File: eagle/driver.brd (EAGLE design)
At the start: 101.6 x 76.2 mm, 39 parts, among them IC1 XMEGA128A1, IC10 ST95P08M, IC11 ST95P08M, IC12 ST95P08M, IC13 ST95P08M, IC14 ST95P08M, IC15 ST95P08M, IC16 74AHC1G32DBV, IC17 74AHC1G32DBV, IC18 74AHC1G08DBV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

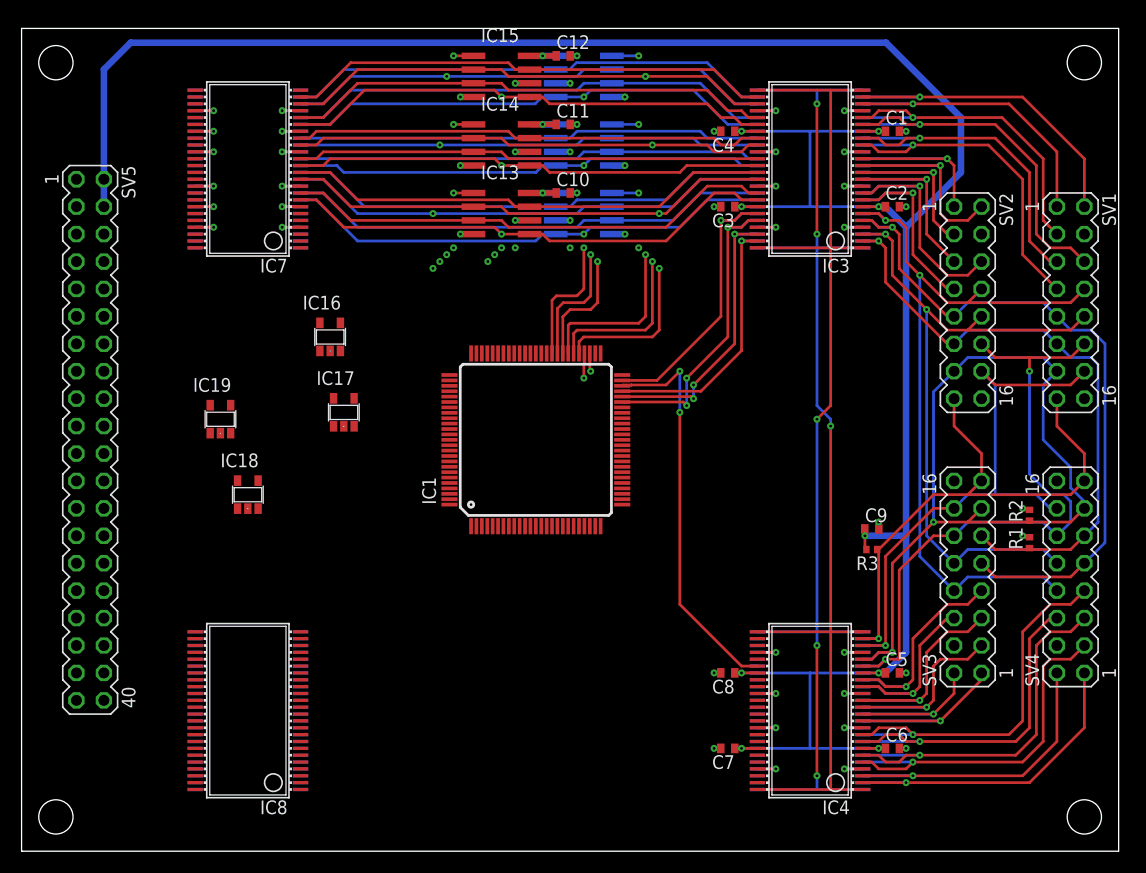
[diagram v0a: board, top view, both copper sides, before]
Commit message: driver board layout progress
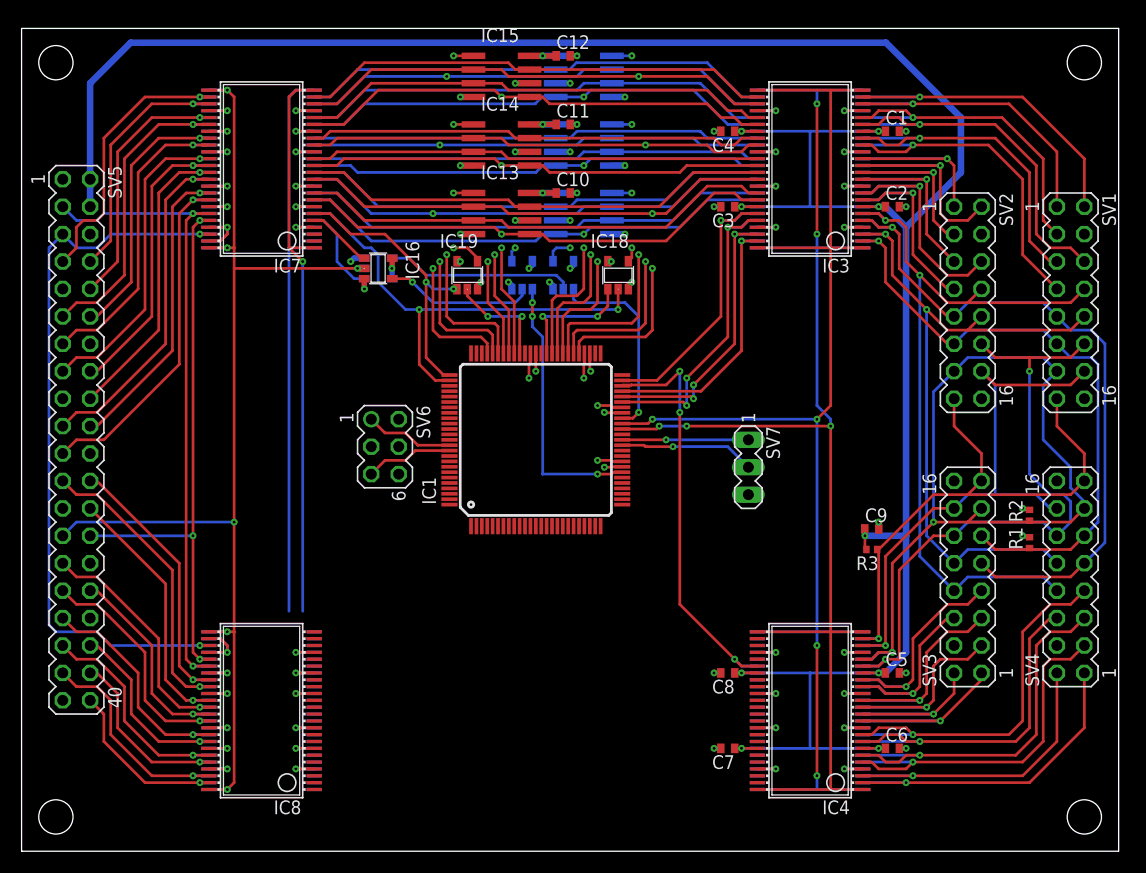
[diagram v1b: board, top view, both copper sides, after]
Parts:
- added IC20, IC21: 74AHC1G02DBV, 74xx-little-us:SOT23-5
- added SV6: (no value), con-lstb:MA03-2
- added SV7: (no value), con-lstb:MA03-1
- moved IC18 39.9 mm to (55.2, 53.3)
- moved IC19 26.5 mm to (41.3, 53.3)
- moved IC17 13.7 mm to (33.0, 54.0), flipped to the bottom, turned to 90 degrees
- moved IC16 7.75 mm to (33.0, 54.0), turned to 270 degrees
- moved IC6 1.27 mm to (22.2, 63.5)
- moved IC7 1.27 mm to (22.2, 62.9)
- moved IC8 1.27 mm to (22.2, 12.7)
- moved IC9 1.27 mm to (22.2, 13.3)
- moved SV5 1.27 mm to (5.08, 38.1)
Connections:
- net N$103 renamed OE
- net N$104 renamed LAT
- removed net N$105: IC4.29, IC5.44
- new net CLK: IC4.29
- new net CLKA: IC1.32, IC21.1
- new net CLKB: IC1.42, IC20.1
- new net CS0: IC10.1, IC11.1, IC12.1, IC18.4
- new net CS1: IC13.1, IC14.1, IC15.1, IC19.4
- new net N$103: IC5.44
- new net N$106: IC8.40, IC9.33, SV5.33
- new net N$108: IC8.43, IC9.30, SV5.35
- new net N$110: IC17.1, IC6.20
- new net N$111: IC8.46, IC9.27, SV5.37
- new net N$113: IC16.1, IC7.5
- new net N$118: IC8.41, IC9.32, SV5.36
- new net N$34: IC6.33, IC7.40, SV5.20
- new net N$46: IC16.4, IC21.2
- new net N$52: IC6.38, IC7.35, SV5.15
- new net SCLK0: IC10.6, IC11.6, IC12.6, IC20.4
- new net SCLK1: IC13.6, IC14.6, IC15.6, IC21.4
- new net VSYNC0: IC1.77, IC18.2, IC6.19
- new net VSYNC1: IC1.76, IC19.1, IC7.6
- net GND: now also IC20.3, IC21.3, IC6.26, IC7.47, IC8.26, IC9.47, SV6.6, SV7.3
- net N$102: now also IC8.38, IC9.35, SV5.31; no longer IC10.6, IC11.6, IC12.6
- net N$109: now also IC8.44, IC9.29, SV5.38; no longer IC13.1, IC14.1, IC15.1
- net N$112: now also IC8.47, IC9.26, SV5.40; no longer IC13.6, IC14.6, IC15.6
- net N$16: now also IC1.40
- net N$19: now also IC1.41
- net N$30: now also IC6.32, IC7.41, SV5.21; no longer IC10.2, IC2.46, IC6.3
- net N$40: now also IC6.35, IC7.38, SV5.19; no longer IC11.2, IC2.40, IC6.9
- net N$42: now also IC17.4, IC20.2; no longer IC10.1, IC11.1, IC12.1
- net N$44: now also IC6.36, IC7.37, SV5.18; no longer IC12.2, IC2.35, IC6.14
- net N$50: now also IC6.37, IC7.36, SV5.16; no longer IC15.5, IC3.30, IC7.19
- net N$54: now also IC6.40, IC7.33, SV5.13; no longer IC14.5, IC3.36, IC7.13
- net N$58: now also IC6.41, IC7.32, SV5.12; no longer IC13.5, IC3.41, IC7.8
- net N$59: now also IC6.43, IC7.30, SV5.11; no longer IC6.23, IC7.2
- net N$60: now also IC6.44, IC7.29, SV5.10; no longer IC6.22, IC7.3
- net N$61: now also IC6.46, IC7.27, SV5.8; no longer IC6.20, IC7.5
- net N$62: now also IC6.47, IC7.26, SV5.7; no longer IC6.19, IC7.6
- net N$87: now also IC1.89, SV6.1; no longer IC8.23, IC9.2
- net N$88: now also IC1.90, SV6.5; no longer IC8.22, IC9.3
- net N$89: now also IC1.38, SV7.1; no longer IC8.20, IC9.5
- net N$90: now also IC1.37, SV7.2; no longer IC8.19, IC9.6
- net N$91: now also IC8.32, IC9.41, SV5.24; no longer IC6.26, IC7.47
- net N$92: now also IC8.27, IC9.46, SV5.5
- net N$93: now also IC8.29, IC9.44, SV5.28
- net N$94: now also IC8.30, IC9.43, SV5.3
- net N$95: now also IC8.33, IC9.40, SV5.23; no longer IC8.26, IC9.47
- net N$96: now also IC8.35, IC9.38, SV5.26; no longer IC8.27, IC9.46
- net N$97: now also IC8.36, IC9.37, SV5.29; no longer IC8.29, IC9.44
- net N$98: now also IC8.37, IC9.36, SV5.32; no longer IC8.30, IC9.43
- net N$99: now also IC16.2, IC17.2, SV5.27
- net PH6: now also IC18.1
- net PJ1: now also IC19.2
- net PJ2: now also IC13.5, IC3.41, IC7.8
- net PJ3: now also IC14.5, IC3.36, IC7.13
- net PJ4: now also IC15.5, IC3.30, IC7.19
- net PJ5: now also IC10.2, IC2.46, IC6.3
- net PJ6: now also IC11.2, IC2.40, IC6.9
- net PJ7: now also IC12.2, IC2.35, IC6.14
- net VCC: now also IC20.5, IC21.5, SV6.2
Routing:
- net N$99: track 0.00 -> 109.2 mm, vias 0 -> 6
- net PJ5: track 0.00 -> 73.5 mm, vias 0 -> 2
- net N$92: track 0.00 -> 68.6 mm, vias 0 -> 2
- net PJ4: track 0.00 -> 68.6 mm, vias 0 -> 2
- net PJ6: track 0.00 -> 65.1 mm, vias 0 -> 2
- net N$94: track 0.00 -> 61.2 mm, vias 0 -> 2
- net PJ7: track 0.00 -> 60.9 mm, vias 0 -> 2
- net PJ3: track 0.00 -> 60.3 mm, vias 0 -> 2
- net PJ2: track 0.00 -> 56.3 mm, vias 0 -> 2
- net N$93: track 0.00 -> 54.0 mm, vias 0 -> 3
- net N$100: track 0.00 -> 53.1 mm, vias 0 -> 1
- net N$101: track 0.00 -> 52.6 mm
- net GND: track 99.5 -> 147.6 mm, vias 45 -> 62
- net VSYNC0: track 0.00 -> 43.7 mm, vias 0 -> 2
- net N$50: track 60.7 -> 27.4 mm, vias 2 -> 1
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
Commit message: board layout progress
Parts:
- removed IC18, IC19: 74AHC1G08DBV, 74xx-little-us:SOT23-5
- moved IC20 0.64 mm to (50.2, 52.7)
- moved IC21 0.64 mm to (46.4, 52.7)
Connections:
- removed net CLK: IC4.29
- removed net CS0: IC10.1, IC11.1, IC12.1, IC18.4
- removed net CS1: IC13.1, IC14.1, IC15.1, IC19.4
- removed net N$103: IC5.44
- net CLKA: now also IC4.29
- net CLKB: now also IC5.44
- net GND: no longer IC18.3, IC19.3
- net LAT: now also IC1.35
- net N$100: now also IC1.78
- net N$101: now also IC1.79
- net N$99: now also IC1.92
- net OE: now also IC1.36
- net PH6: no longer IC18.1
- net PJ1: no longer IC19.2
- net VCC: no longer IC18.5, IC19.5
- net VSYNC0: now also IC10.1, IC11.1, IC12.1; no longer IC18.2
- net VSYNC1: now also IC13.1, IC14.1, IC15.1; no longer IC19.1
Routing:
- net LAT: track 0.00 -> 29.3 mm, vias 0 -> 3
- net OE: track 0.00 -> 28.6 mm, vias 0 -> 3
- net CS1: track 26.2 -> 0.00 mm, vias 4 -> 0
- net VSYNC0: track 43.7 -> 68.8 mm, vias 2 -> 5
- net CS0: track 24.7 -> 0.00 mm, vias 4 -> 0
- net VSYNC1: track 26.3 -> 51.0 mm, vias 2 -> 4
- net N$99: track 109.2 -> 130.2 mm
- net N$101: track 52.6 -> 67.4 mm, vias 0 -> 1
- net N$100: track 53.1 -> 66.7 mm, vias 1 -> 2
- net VCC: track 51.8 -> 65.2 mm, vias 20 -> 24
- net PH6: track 11.6 -> 0.00 mm, vias 2 -> 0
- net PJ1: track 10.0 -> 0.00 mm, vias 2 -> 0
- net GND: track 147.6 -> 156.5 mm, vias 62 -> 66
- net CLKB: track 18.3 -> 26.5 mm
- net PH5: track 57.6 -> 56.5 mm
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
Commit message: board layout progress
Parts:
- added IC18, IC19: 74AHC1G125DBV, 74xx-little-us:SOT23-5
- added IC22, IC23, IC24, IC25: ST95P08M, st-microelectronics:SO08
- added R4, R5: 33k, rcl:R0402
- IC16, IC17: value 74AHC1G32DBV -> 74AHC1G02DBV
- IC20, IC21: value 74AHC1G02DBV -> ST95P08M; device 74xx-little-us:SOT23-5 -> st-microelectronics:SO08
- moved IC21 42.0 mm to (44.5, 10.8), flipped to the top, turned to 270 degrees
- moved IC20 36.0 mm to (44.5, 17.1), flipped to the top, turned to 270 degrees
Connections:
- removed net CLKA: IC1.32, IC21.1, IC4.29
- removed net CLKB: IC1.42, IC20.1, IC5.44
- removed net N$100: IC1.78, IC7.1, IC7.24, IC9.1, IC9.24
- removed net N$101: IC1.79, IC6.1, IC6.24, IC8.1, IC8.24
- removed net N$75: IC5.26, IC9.23
- removed net N$77: IC5.29, IC9.20
- removed net N$79: IC5.32, IC9.17
- removed net N$81: IC5.35, IC9.14
- removed net N$83: IC5.37, IC9.12
- removed net N$85: IC5.40, IC9.9
- new net CLK_EN0: IC1.80, IC19.1
- new net CLK_EN1: IC1.81, IC18.1
- new net N$48: IC1.78, IC6.1, IC6.24, IC9.1, IC9.24
- new net N$56: IC1.79, IC7.1, IC7.24, IC8.1, IC8.24
- new net PB0: IC1.5, IC25.5, IC5.37, IC9.12
- new net PB1: IC1.6, IC24.5, IC5.32, IC9.17
- new net PB2: IC1.7, IC23.5, IC5.26, IC9.23
- new net PB3: IC1.8, IC25.2, IC5.40, IC9.9
- new net PB4: IC1.9, IC24.2, IC5.35, IC9.14
- new net PB5: IC1.10, IC23.2, IC5.29, IC9.20
- new net PB6: IC1.11
- new net PB7: IC1.12
- new net VSYNC2: IC1.1, IC20.1, IC21.1, IC22.1, IC8.19
- new net VSYNC3: IC1.2, IC23.1, IC24.1, IC25.1, IC9.6
- net GND: now also IC18.3, IC19.3, IC20.4, IC21.4, IC22.4, IC23.4, IC24.4, IC25.4; no longer IC20.3, IC21.3
- net N$110: now also R4.1
- net N$113: now also R5.1
- net N$16: now also IC3.1, IC3.24, IC3.25, IC3.48; no longer IC2.1, IC2.24, IC2.25, IC2.48
- net N$19: now also IC2.1, IC2.24, IC2.25, IC2.48; no longer IC3.1, IC3.24, IC3.25, IC3.48
- net N$42: now also IC16.4, IC18.2; no longer IC17.4, IC20.2
- net N$46: now also IC17.4, IC19.2; no longer IC16.4, IC21.2
- net N$63: now also IC22.5
- net N$64: now also IC22.3
- net N$65: now also IC22.7
- net N$66: now also IC22.2
- net N$67: now also IC21.5
- net N$68: now also IC21.3
- net N$69: now also IC21.2
- net N$70: now also IC21.7
- net N$71: now also IC20.5
- net N$72: now also IC20.3
- net N$73: now also IC20.2
- net N$74: now also IC20.7
- net N$76: now also IC23.3
- net N$78: now also IC23.7
- net N$80: now also IC24.3
- net N$82: now also IC24.7
- net N$84: now also IC25.3
- net N$86: now also IC25.7
- net SCLK0: now also IC1.32, IC19.4, IC23.6, IC24.6, IC25.6, IC5.44; no longer IC20.4
- net SCLK1: now also IC1.42, IC18.4, IC20.6, IC21.6, IC22.6, IC4.29; no longer IC21.4
- net VCC: now also IC18.5, IC19.5, IC20.8, IC21.8, IC22.8, IC23.8, IC24.8, IC25.8, R4.2, R5.2; no longer IC20.5, IC21.5
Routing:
- net SCLK1: track 21.2 -> 127.9 mm, vias 4 -> 14
- net SCLK0: track 22.5 -> 116.8 mm, vias 4 -> 9
- net N$56: track 0.00 -> 88.3 mm, vias 0 -> 3
- net N$48: track 0.00 -> 88.2 mm, vias 0 -> 1
- net PB2: track 0.00 -> 75.1 mm, vias 0 -> 2
- net PB5: track 0.00 -> 70.8 mm, vias 0 -> 2
- net N$101: track 67.4 -> 0.00 mm, vias 1 -> 0
- net N$100: track 66.7 -> 0.00 mm, vias 2 -> 0
- net PB1: track 0.00 -> 66.7 mm, vias 0 -> 2
- net PB4: track 0.00 -> 62.2 mm, vias 0 -> 2
- net VSYNC3: track 0.00 -> 61.3 mm, vias 0 -> 4
- net PB0: track 0.00 -> 60.9 mm, vias 0 -> 2
- net PB3: track 0.00 -> 56.6 mm, vias 0 -> 2
- net VSYNC2: track 0.00 -> 45.0 mm, vias 0 -> 3
- net N$63: track 0.00 -> 44.7 mm
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
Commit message: board layout progress
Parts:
- moved R5 0.90 mm to (29.2, 56.5)
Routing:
- net PH0: track 62.8 -> 59.4 mm
- net PH1: track 67.3 -> 64.2 mm
- net PH2: track 75.0 -> 72.0 mm
- net PJ7: track 60.9 -> 58.7 mm
- net PJ6: track 64.9 -> 62.9 mm
- net PJ5: track 73.2 -> 71.3 mm
- net VCC/2: track 241.5 -> 242.1 mm

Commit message: board layout progress
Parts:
- added C13, C14, C15: 100n, rcl:C0402
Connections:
- removed net N$63: IC22.5, IC4.47, IC8.2
- removed net N$66: IC22.2, IC4.44, IC8.5
- removed net N$67: IC21.5, IC4.41, IC8.8
- removed net N$69: IC21.2, IC4.38, IC8.11
- removed net N$71: IC20.5, IC4.36, IC8.13
- removed net N$73: IC20.2, IC4.33, IC8.16
- new net PC0: IC1.15, IC22.2, IC4.44, IC8.5
- new net PC1: IC1.16, IC21.2, IC4.38, IC8.11
- new net PC2: IC1.17, IC20.2, IC4.33, IC8.16
- new net PC3: IC1.18, IC22.5, IC4.47, IC8.2
- new net PC4: IC1.19, IC21.5, IC4.41, IC8.8
- new net PC5: IC1.20, IC20.5, IC4.36, IC8.13
- new net PC6: IC1.21
- new net PC7: IC1.22
- net GND: now also C13.2, C14.2, C15.2
- net VCC: now also C13.1, C14.1, C15.1
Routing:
- net PC3: track 0.00 -> 76.2 mm, vias 0 -> 2
- net PC0: track 0.00 -> 71.5 mm, vias 0 -> 2
- net PC4: track 0.00 -> 68.3 mm, vias 0 -> 2
- net PC1: track 0.00 -> 62.9 mm, vias 0 -> 2
- net PC5: track 0.00 -> 62.0 mm, vias 0 -> 2
- net PC2: track 0.00 -> 57.9 mm, vias 0 -> 2
- net N$63: track 44.7 -> 0.00 mm
- net N$66: track 44.2 -> 0.00 mm
- net N$73: track 43.7 -> 0.00 mm
- net N$71: track 43.2 -> 0.00 mm
- net N$67: track 43.2 -> 0.00 mm
- net N$69: track 42.1 -> 0.00 mm
- net VCC: track 74.2 -> 78.0 mm
- net GND: track 164.9 -> 168.6 mm, vias 72 -> 75
- net OE: track 28.6 -> 26.0 mm, vias 3 -> 1
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
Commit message: board layout progress
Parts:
- added C16, C17, C18, C19: 100n, rcl:C0402
- added R10, R6, R7, R8, R9: 47k, rcl:R0402
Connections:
- net GND: now also C16.2, C17.2, C18.2, C19.2, R10.2, R6.1, R7.1, R8.1, R9.1
- net N$11: now also R9.2
- net N$12: now also R10.1
- net N$15: now also R8.2
- net N$17: now also R7.2
- net N$27: now also R6.2
- net VCC: now also C16.1, C17.1, C18.1, C19.1
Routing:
- net GND: track 168.6 -> 174.6 mm, vias 75 -> 84
- net VCC: track 78.0 -> 80.5 mm, vias 28 -> 32
- net N$99: track 130.2 -> 130.7 mm

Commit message: board layout progress
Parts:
- added C20, C21, C22, C23: 100n, rcl:C0402
- added R11, R12, R13, R14, R15, R16, R17, R18, R19, R20, R21, R22, R23, R24, R25, R26, R27, R28, R29, R30, R31, R32, R33, R34: 33k, rcl:R0402
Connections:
- net GND: now also C20.2, C21.2, C22.2, C23.2
- net N$29: now also R11.1
- net N$31: now also R12.2
- net N$35: now also R15.1
- net N$41: now also R13.2
- net N$43: now also R16.1
- net N$45: now also R14.2
- net N$47: now also R17.1
- net N$49: now also R18.2
- net N$51: now also R19.1
- net N$53: now also R20.2
- net N$55: now also R21.1
- net N$57: now also R22.2
- net N$64: now also R28.2
- net N$65: now also R27.1
- net N$68: now also R26.2
- net N$70: now also R25.1
- net N$72: now also R24.2
- net N$74: now also R23.1
- net N$76: now also R30.2
- net N$78: now also R29.1
- net N$80: now also R32.2
- net N$82: now also R31.1
- net N$84: now also R34.2
- net N$86: now also R33.1
- net PB7: now also R29.2, R30.1, R31.2, R32.1, R33.2, R34.1
- net PC7: now also R23.2, R24.1, R25.2, R26.1, R27.2, R28.1
- net PH6: now also R17.2, R18.1, R19.2, R20.1, R21.2, R22.1
- net PH7: now also R11.2, R12.1, R13.1, R14.1, R15.2, R16.2
- net VCC: now also C20.1, C21.1, C22.1, C23.1
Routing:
- net PB7: track 0.00 -> 48.8 mm, vias 0 -> 8
- net PH6: track 0.00 -> 48.1 mm, vias 0 -> 8
- net PH7: track 0.00 -> 45.7 mm, vias 0 -> 6
- net PC7: track 0.00 -> 36.2 mm, vias 0 -> 7
- net GND: track 174.6 -> 180.2 mm, vias 84 -> 96
- net VCC: track 80.5 -> 83.0 mm
- net VCC/2: track 242.1 -> 240.6 mm
- net N$84: track 43.2 -> 43.8 mm
- net N$82: track 42.1 -> 42.8 mm
- net N$80: track 42.1 -> 42.8 mm
- net N$78: track 44.2 -> 44.9 mm
- net N$76: track 44.2 -> 44.9 mm
- net N$53: track 41.6 -> 42.3 mm
- net N$43: track 43.7 -> 44.4 mm
- net N$41: track 41.6 -> 42.3 mm
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- added copper zone on layer 1, net GND
- added copper zone on layer 16, net GND

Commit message: finalizing board layout
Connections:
- net GND: now also IC8.27, IC8.29, IC9.44, IC9.46
- net N$92: no longer IC8.27, IC9.46
- net N$93: no longer IC8.29, IC9.44
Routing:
- net N$92: track 68.6 -> 15.4 mm, vias 2 -> 1
- net N$93: track 54.0 -> 40.7 mm, vias 3 -> 2
- net GND: track 180.2 -> 187.5 mm
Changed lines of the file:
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@@
 <wire x1="17.3482" y1="11.43" x2="19.05" y2="11.43" width="0.254" layer="16"/>
 <wire x1="17.3482" y1="14.605" x2="19.05" y2="14.605" width="0.254" layer="16"/>
-<wire x1="17.3482" y1="18.415" x2="19.05" y2="18.415" width="0.254" layer="16"/>
 <wire x1="27.1018" y1="18.415" x2="25.4" y2="18.415" width="0.254" layer="16"/>
 <wire x1="27.1018" y1="14.605" x2="25.4" y2="14.605" width="0.254" layer="16"/>
@@
 <via x="67.31" y="73.025" extent="1-16" drill="0.254"/>
 <via x="78.74" y="73.025" extent="1-16" drill="0.254"/>
+<contactref element="IC8" pad="27"/>
+<contactref element="IC9" pad="46"/>
+<contactref element="IC8" pad="29"/>
+<contactref element="IC9" pad="44"/>
+<wire x1="17.3482" y1="17.78" x2="18.415" y2="17.78" width="0.254" layer="1"/>
+<wire x1="18.415" y1="17.78" x2="19.05" y2="18.415" width="0.254" layer="1"/>
+<wire x1="17.3482" y1="19.05" x2="19.05" y2="19.05" width="0.254" layer="1"/>
+<wire x1="17.3482" y1="19.05" x2="19.05" y2="19.05" width="0.254" layer="16"/>
+<wire x1="17.3482" y1="18.415" x2="19.05" y2="18.415" width="0.254" layer="16"/>
+<wire x1="17.3482" y1="17.78" x2="18.415" y2="17.78" width="0.254" layer="16"/>
+<wire x1="18.415" y1="17.78" x2="19.05" y2="18.415" width="0.254" layer="16"/>
 </signal>
 <signal name="VCC">
@@
 <via x="16.51" y="57.15" extent="1-16" drill="0.254"/>
 <wire x1="17.3482" y1="57.15" x2="16.51" y2="57.15" width="0.254" layer="1"/>
-<contactref element="IC8" pad="27"/>
-<contactref element="IC9" pad="46"/>
-<wire x1="3.81" y1="57.15" x2="2.54" y2="55.88" width="0.254" layer="16"/>
-<wire x1="2.54" y1="55.88" x2="2.54" y2="20.955" width="0.254" layer="16"/>
-<wire x1="2.54" y1="20.955" x2="3.175" y2="20.32" width="0.254" layer="16"/>
-<wire x1="3.175" y1="20.32" x2="6.985" y2="20.32" width="0.254" layer="16"/>
-<wire x1="6.985" y1="20.32" x2="8.255" y2="19.05" width="0.254" layer="16"/>
-<wire x1="8.255" y1="19.05" x2="16.51" y2="19.05" width="0.254" layer="16"/>
-<wire x1="16.51" y1="19.05" x2="17.3482" y2="19.05" width="0.254" layer="16"/>
 <wire x1="3.81" y1="57.15" x2="5.08" y2="55.88" width="0.254" layer="16"/>
 <wire x1="5.08" y1="55.88" x2="6.985" y2="55.88" width="0.254" layer="16"/>
 <wire x1="6.985" y1="55.88" x2="8.255" y2="57.15" width="0.254" layer="16"/>
 <wire x1="8.255" y1="57.15" x2="16.51" y2="57.15" width="0.254" layer="16"/>
-<wire x1="17.3482" y1="19.05" x2="16.51" y2="19.05" width="0.254" layer="1"/>
-<via x="16.51" y="19.05" extent="1-16" drill="0.254"/>
 </signal>
 <signal name="N$93">
@@
 <via x="16.51" y="58.42" extent="1-16" drill="0.254"/>
 <wire x1="17.3482" y1="58.42" x2="16.51" y2="58.42" width="0.254" layer="16"/>
-<contactref element="IC8" pad="29"/>
-<contactref element="IC9" pad="44"/>
-<wire x1="15.875" y1="29.21" x2="15.875" y2="18.415" width="0.254" layer="1"/>
-<wire x1="15.875" y1="18.415" x2="16.51" y2="17.78" width="0.254" layer="1"/>
-<wire x1="16.51" y1="17.78" x2="17.3482" y2="17.78" width="0.254" layer="1"/>
-<via x="16.51" y="17.78" extent="1-16" drill="0.254"/>
-<wire x1="17.3482" y1="17.78" x2="16.51" y2="17.78" width="0.254" layer="16"/>
 </signal>
 <signal name="N$35">
